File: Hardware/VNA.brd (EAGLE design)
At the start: 122 x 96 mm, 513 parts, among them IC1 ADL5801, IC10 LT5560, IC11 THS4521IDGKR, IC12 MCP33131D-10-E/MS, IC13 SI5351C, IC14 MAX2871, IC15 NCP702-3.3, IC16 RFSW6042, IC17 AP2114H, IC18 RFSW6042, IC19 MAX2871, IC2 LT5560, IC20 NCP702-3.3, IC21 AP2114H, IC22 QPC6324, IC23 RFSA3714, IC24 TRF37A73, IC25 QPC6324, IC26 QPC6324, IC27 QPC6324, IC28 LDL212PU50R, IC29 LDL212PU50R, IC3 THS4521IDGKR, IC30 LDL212PU50R, IC31 LDL212PU50R, IC32 TPS65265, IC34 NCP702-1.8, IC35 NCP702-1.8, IC36 NCP702-1.8, IC37 ADL5801, IC4 MCP33131D-10-E/MS, IC5 ADL5801, IC6 LT5560, IC7 THS4521IDGKR, IC8 MCP33131D-10-E/MS, IC9 STM32G431CB, J1 AMPHENOL_132289, J2 AMPHENOL_132289, J3 DCJ0202, J4 TYPE-C16P(073), Q1 FA-128 26MHz, T1 B012-617DB-1-63-B331, T2 B012-617DB-1-63-B331, T3 B012-617DB-1-63-B331, U2 6SLX9TQG144, U4 W25Q16BVSN, X4 DNP

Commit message: library update
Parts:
- C1, C10, C100, C101, C102, C103, C104, C105, C107, C108, C109, C11, C110, C111, C112, C114, C115, C116, C117, C118, C119, C12, C120, C121, C122, C127, C128, C129, C13, C130, C131, C132, C133, C134, C135, C136, C137, C138, C14, C143, C144, C145, C146, C147, C148, C149, C15, C150, C151, C152, C153, C154, C155, C156, C157, C16, C167, C17, C175, C176, C178, C179, C18, C182, C183, C186, C187, C188, C19, C191, C192, C193, C194, C195, C196, C197, C198, C199, C2, C20, C200, C201, C202, C203, C204, C205, C206, C207, C208, C209, C21, C210, C211, C212, C213, C214, C215, C216, C217, C218, C219, C22, C220, C221, C222, C223, C224, C225, C226, C227, C228, C23, C24, C25, C26, C27, C28, C29, C3, C30, C31, C32, C33, C34, C35, C36, C37, C38, C39, C4, C40, C41, C42, C43, C44, C45, C46, C47, C48, C49, C5, C50, C51, C52, C53, C54, C55, C56, C57, C58, C59, C6, C60, C61, C62, C63, C64, C65, C66, C67, C68, C69, C7, C70, C71, C72, C73, C74, C75, C76, C77, C78, C79, C8, C80, C81, C82, C83, C84, C85, C86, C87, C88, C89, C9, C90, C91, C92, C93, C94, C95, C96, C97, C98, C99: device rcl:C0402 -> VNA:C0402
- D1, D2: device diodes:SMB -> VNA:SMB
- IC1, IC37, IC5: device rf:QFN50P400X400X100-25T250N -> VNA:QFN50P400X400X100-25T250N
- IC11, IC3, IC7: device rf:MSOP8 -> VNA:MSOP8
- IC22, IC25, IC26, IC27: device rf:QFN50P400X400X75-21T206 -> VNA:QFN50P400X400X75-21T206
- IC23: device rf:QFN50P400X400X75-25T270 -> VNA:QFN50P400X400X75-25T270
- IC9: device custom-ic:QFN50P700X700X60-49T560N -> VNA:QFN50P700X700X60-49T560N
- J1, J2: device custom-connectors:AMPHENOL_132289 -> VNA:AMPHENOL_132289
- J4: device custom-connectors:TYPE-C16P -> VNA:TYPE-C16P
- JP1: device pinhead:2X10 -> VNA:2X10
- JP2: device pinhead:1X10/90 -> VNA:1X10/90
- L1, L10, L11, L12, L13, L14, L15, L16, L17, L18, L19, L2, L20, L21, L22, L23, L24, L25, L26, L27, L28, L3, L31, L32, L33, L34, L35, L36, L37, L38, L39, L4, L40, L41, L42, L43, L44, L45, L46, L47, L48, L49, L5, L50, L6, L7, L8, L9: device rf:R0402 -> VNA:R0402:1
- LED1, LED10, LED2, LED3, LED4, LED5, LED6, LED7, LED8, LED9: device led:CHIPLED_0603 -> VNA:CHIPLED_0603
- R1, R10, R100, R101, R102, R103, R104, R105, R106, R107, R108, R109, R11, R110, R111, R112, R113, R114, R115, R116, R117, R118, R119, R12, R120, R121, R122, R123, R124, R125, R126, R127, R128, R129, R13, R130, R131, R132, R133, R134, R135, R136, R137, R138, R139, R14, R140, R141, R142, R143, R144, R145, R146, R147, R148, R15, R16, R17, R18, R19, R2, R20, R21, R22, R23, R24, R25, R26, R27, R28, R29, R3, R30, R31, R32, R33, R34, R35, R36, R37, R38, R39, R4, R40, R41, R42, R43, R44, R45, R46, R47, R48, R49, R5, R50, R51, R52, R53, R54, R55, R56, R57, R58, R59, R6, R60, R61, R62, R63, R64, R65, R66, R67, R69, R7, R70, R71, R72, R73, R74, R75, R76, R77, R78, R79, R8, R80, R81, R82, R83, R84, R85, R86, R87, R88, R89, R9, R90, R91, R92, R93, R94, R95, R96, R97, R98, R99: device rcl:R0402 -> VNA:R0402
- T1, T2, T3: device rf:EASTEVER_BALUN -> VNA:EASTEVER_BALUN
- TP1, TP10, TP11, TP12, TP13, TP14, TP15, TP16, TP17, TP18, TP19, TP2, TP3, TP4, TP5, TP6, TP7, TP8, TP9: device testpad:B1,27 -> VNA:B1,27
- X5, X6: value (none) -> SMA_CONNECTOR

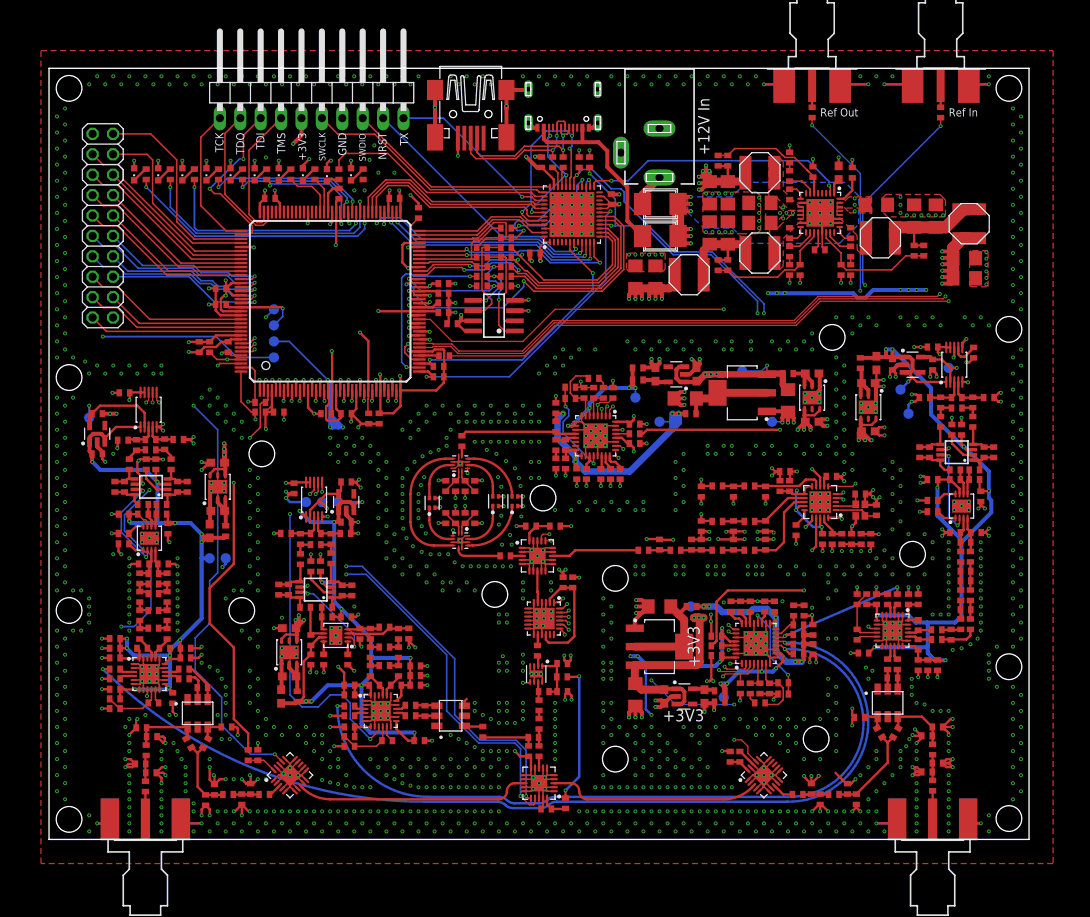
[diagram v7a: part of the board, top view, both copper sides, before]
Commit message: reworked power supply section
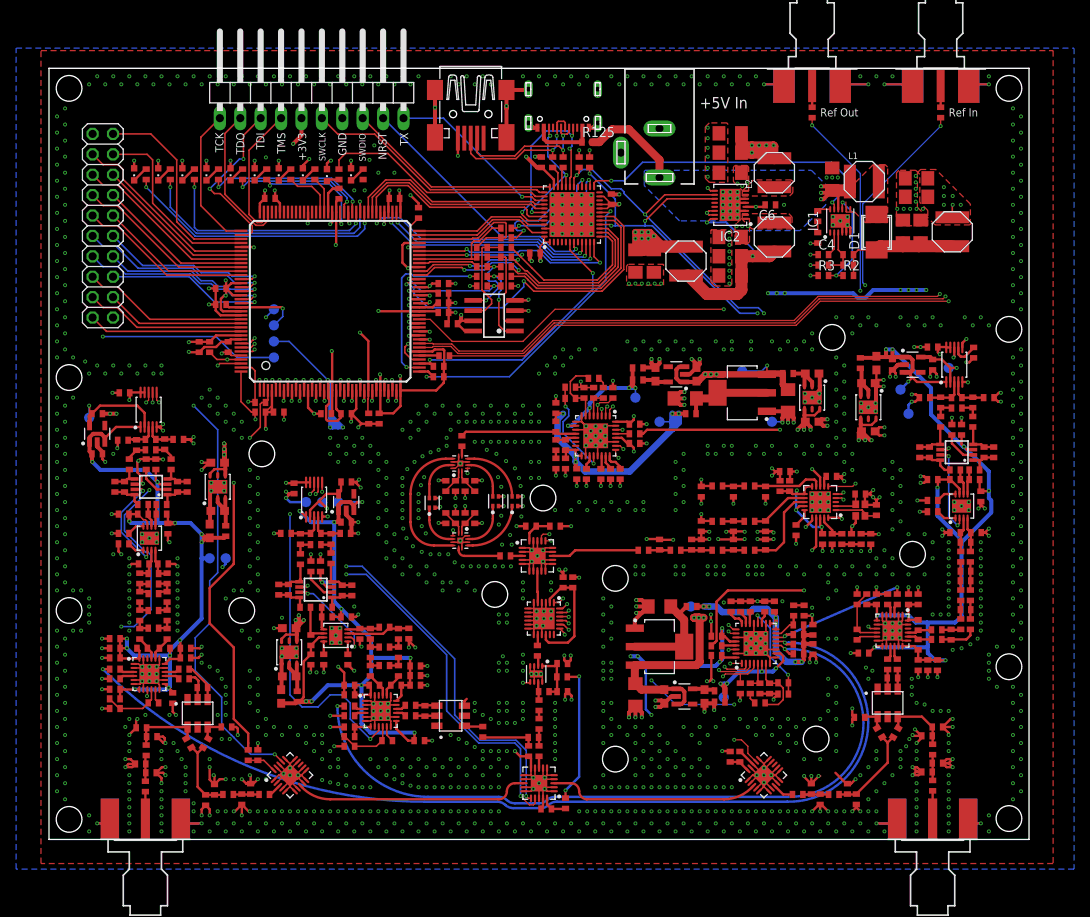
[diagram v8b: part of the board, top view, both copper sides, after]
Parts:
- removed C223: 56p, VNA:C0402
- removed C224, C225, C226, C227, C228: 100n, VNA:C0402
- removed D2: MBRS2040LT3G, VNA:SMB
- removed L54: 6u8, VNA:SRN5040
- removed L55: 10u, VNA:SRN5040
- removed R143, R144, R145, R146, R147: 0, VNA:R0402
- removed R148: 330, VNA:R0402
- added IC33: ADL5801, VNA:QFN50P400X400X100-25T250N
- added L29: Ferrite, VNA:R0402:1
- added L30: 330n, VNA:R0402:1
- added R68: 620, VNA:R0402
- C1, C2, C3: value 100n/RF -> 10u; device VNA:C0402 -> VNA:C1206
- C10, C11, C8: value 10n -> 10u; device VNA:C0402 -> VNA:C1206
- C100: value 18p -> 1u
- C101: value 56p -> 1u
- C102, C103, C118, C97: value 18p -> 100n
- C104, C105, C120, C143, C148, C157, C191, C192, C30, C39, C80: value 100n -> 10n
- C106, C123, C160: value 1u -> 10n; device VNA:C0603 -> VNA:C0402
- C107: value 10n -> DNP
- C108: value 4p -> 1u
- C109: value 4p -> 100n/RF
- C110, C71, C96: value 100n -> 100n/RF
- C111: value 56p -> 10n
- C112: value 18p -> DNP
- C113: value 4u7 -> DNP; device VNA:C0603 -> VNA:C0402
- C114, C115, C116, C122, C134, C193, C73: value 1u -> 100n
- C117, C135, C222: value 180p -> 100n
- C119: value 3n3 -> 100n
- C12, C13, C15, C49, C7: value 100n -> 10u; device VNA:C0402 -> VNA:C1206
- C121: value 100n/RF -> 330p
- C124: value 1u -> 120p; device VNA:C0603 -> VNA:C0402
- C125, C126: value 10u -> 330p; device VNA:C1206 -> VNA:C0402
- C127: value 100n -> 330p
- C128, C196: value 100n -> 150p
- C129, C131, C138, C145, C198, C203, C59: value 100n -> 1u
- C130: value 10n -> 33p
- C132, C153, C33, C4: value 100n/RF -> 100n
- C133: value 1u -> 100n/RF
- C136, C99: value 18p -> 100n/RF
- C137: value 3n3 -> 1u
- C139, C140: value 1u -> 100n; device VNA:C0603 -> VNA:C0402
- C14: value 120p -> 10u; device VNA:C0402 -> VNA:C1206
- C141, C142: value 10u -> 10n; device VNA:C1206 -> VNA:C0402
- C144, C149: value 100n -> DNP
- C146, C147, C65, C74: value 10n -> 100n/RF
- C150: value 100n/RF -> DNP
- C158, C162, C164: value 1u -> 330p; device VNA:C0603 -> VNA:C0402
- C159: value 4u7 -> 100n; device VNA:C0603 -> VNA:C0402
- C16, C17, C53: value 330p -> 10u; device VNA:C0402 -> VNA:C1206
- C161: value 4u7 -> 120p; device VNA:C0603 -> VNA:C0402
- C163: value 4u7 -> 330p; device VNA:C0603 -> VNA:C0402
- C165: value 1u -> 150p; device VNA:C0603 -> VNA:C0402
- C166, C168: device VNA:C0603 -> VNA:C0402
- C167, C197: value 100n -> 33p
- C169, C181, C190: value 22u -> 100n; device VNA:C1206 -> VNA:C0402
- C170: value 22u -> 100n/RF; device VNA:C1206 -> VNA:C0402
- C171, C172, C180: value 22u -> 10n; device VNA:C1206 -> VNA:C0402
- C173: value 10u/25V -> DNP; device VNA:C1206 -> VNA:C0402
- C174: value 22u -> DNP; device VNA:C1206 -> VNA:C0402
- C175: value 47n -> 10n
- C176: value 1n -> DNP
- C177: value 10u/25V -> 1u; device VNA:C1206 -> VNA:C0402
- C178: value 47n -> 100n/RF
- C179: value 8p2 -> 100n/RF
- C18, C26, C52, C81: value 100n -> 1u; device VNA:C0402 -> VNA:C0603
- C182, C56: value 120p -> 100n
- C183, C69, C83: value DNP -> 100n
- C184, C189: value 22u -> 330p; device VNA:C1206 -> VNA:C0402
- C185: value 10u/25V -> 100n; device VNA:C1206 -> VNA:C0402
- C186: value 47n -> 100n
- C187: value 510p -> 330p
- C188: value DNP -> 330p
- C19, C27: value 330p -> 1u; device VNA:C0402 -> VNA:C0603
- C194: value 1u -> 120p
- C20, C21, C28, C79: device VNA:C0402 -> VNA:C0603
- C200, C201, C213, C214, C215, C217, C218, C219, C55, C72: value 10n -> 100n
- C202, C87: value 10n -> 1u
- C22, C23: value 100n -> 4u7; device VNA:C0402 -> VNA:C0603
- C221, C98: value 56p -> 100n
- C24, C25: value DNP -> 4u7; device VNA:C0402 -> VNA:C0603
- C31: value 150p -> 4p
- C32: value 33p -> 100n
- C34: value 100n/RF -> 4p
- C35, C36, C67: value 100n/RF -> 18p
- C37: value DNP -> 18p
- C38: value 100n -> 56p
- C40, C42: value 10n -> 56p
- C41, C47: value 1u -> 56p
- C43: value 100n -> 180p
- C44, C45: value 100n -> 18p
- C46, C95: value 1u -> 18p
- C5, C51: value DNP -> 10n
- C50: value DNP -> 1u; device VNA:C0402 -> VNA:C0603
- C57: value 150p -> 100n
- C58: value 33p -> 1u
- C60: value 330p -> 1u
- C61, C62, C85, C94: value 330p -> 100n
- C63: value 1u -> 180p
- C66: value 100n/RF -> 3n3
- C78: value 1u -> 10u; device VNA:C0402 -> VNA:C1206
- C82: value DNP -> 10u; device VNA:C0402 -> VNA:C1206
- C88: value 120p -> 1u
- C89: value 150p -> 1u
- C9: value 1u -> 100p
- C90: value 33p -> 180p
- C92: value 330p -> 3n3
- C93: value 330p -> 10n
- IC1: value ADL5801 -> MIC2253; device VNA:QFN50P400X400X100-25T250N -> VNA:SON50P300X300X90-13T170X240N
- IC10: value LT5560 -> MAX2871; device VNA:SON50P300X300X80-9T165X238 -> VNA:QFN50P500X500X80-33T310
- IC11: value THS4521IDGKR -> RFSW6042; device VNA:MSOP8 -> VNA:QFN40P180X180X55-13T76N
- IC12: value MCP33131D-10-E/MS -> RFSW6042; device VNA:SOP50P490X110-10N -> VNA:QFN40P180X180X55-13T76N
- IC13: value SI5351C -> QPC6324; device VNA:QFN50P400X400X90-21T270N -> VNA:QFN50P400X400X75-21T206
- IC14: value MAX2871 -> RFSA3714; device VNA:QFN50P500X500X80-33T310 -> VNA:QFN50P400X400X75-25T270
- IC15: value NCP702-3.3 -> TRF37A73; device VNA:SOT95P240X110-5 -> VNA:SON50P200X200X80-9T90X160N
- IC16, IC18: value RFSW6042 -> QPC6324; device VNA:QFN40P180X180X55-13T76N -> VNA:QFN50P400X400X75-21T206
- IC17: value AP2114H -> QPC6324; device VNA:SOT230P700X180-4 -> VNA:QFN50P400X400X75-21T206
- IC19: value MAX2871 -> AP2114H; device VNA:QFN50P500X500X80-33T310 -> VNA:SOT230P700X180-4
- IC2: value LT5560 -> LM3370SD-4221; device VNA:SON50P300X300X80-9T165X238 -> VNA:SON50P400X500X80-17T260X400N
- IC21: value AP2114H -> MAX2871; device VNA:SOT230P700X180-4 -> VNA:QFN50P500X500X80-33T310
- IC22, IC27: value QPC6324 -> LT5560; device VNA:QFN50P400X400X75-21T206 -> VNA:SON50P300X300X80-9T165X238
- IC23: value RFSA3714 -> THS4521IDGKR; device VNA:QFN50P400X400X75-25T270 -> VNA:MSOP8
- IC24: value TRF37A73 -> ADL5801; device VNA:SON50P200X200X80-9T90X160N -> VNA:QFN50P400X400X100-25T250N
- IC25: value QPC6324 -> NCP702-1.8; device VNA:QFN50P400X400X75-21T206 -> VNA:SOT95P240X110-5
- IC26: value QPC6324 -> MCP33131D-10-E/MS; device VNA:QFN50P400X400X75-21T206 -> VNA:SOP50P490X110-10N
- IC28: value LDL212PU50R -> THS4521IDGKR; device VNA:SON95P300X300X100-7T170X240N -> VNA:MSOP8
- IC29: value LDL212PU50R -> ADL5801; device VNA:SON95P300X300X100-7T170X240N -> VNA:QFN50P400X400X100-25T250N
- IC3: value THS4521IDGKR -> LDL212PU50R; device VNA:MSOP8 -> VNA:SON95P300X300X100-7T170X240N
- IC30: value LDL212PU50R -> NCP702-1.8; device VNA:SON95P300X300X100-7T170X240N -> VNA:SOT95P240X110-5
- IC31: value LDL212PU50R -> MCP33131D-10-E/MS; device VNA:SON95P300X300X100-7T170X240N -> VNA:SOP50P490X110-10N
- IC32: value TPS65265 -> THS4521IDGKR; device VNA:QFN50P500X500X100-33T345N -> VNA:MSOP8
- IC35: value NCP702-1.8 -> MCP33131D-10-E/MS; device VNA:SOT95P240X110-5 -> VNA:SOP50P490X110-10N
- IC36: value NCP702-1.8 -> LT5560; device VNA:SOT95P240X110-5 -> VNA:SON50P300X300X80-9T165X238
- IC37: value ADL5801 -> STM32G431CB; device VNA:QFN50P400X400X100-25T250N -> VNA:QFN50P700X700X60-49T560N
- IC4: value MCP33131D-10-E/MS -> LDL212PU50R; device VNA:SOP50P490X110-10N -> VNA:SON95P300X300X100-7T170X240N
- IC5: value ADL5801 -> LDL212PU50R; device VNA:QFN50P400X400X100-25T250N -> VNA:SON95P300X300X100-7T170X240N
- IC6: value LT5560 -> LDL212PU50R; device VNA:SON50P300X300X80-9T165X238 -> VNA:SON95P300X300X100-7T170X240N
- IC7: value THS4521IDGKR -> SI5351C; device VNA:MSOP8 -> VNA:QFN50P400X400X90-21T270N
- IC8: value MCP33131D-10-E/MS -> AP2114H; device VNA:SOP50P490X110-10N -> VNA:SOT230P700X180-4
- IC9: value STM32G431CB -> NCP702-3.3; device VNA:QFN50P700X700X60-49T560N -> VNA:SOT95P240X110-5
- J1: value AMPHENOL_132289 -> DNP; device VNA:AMPHENOL_132289 -> VNA:DCJ0202
- J3: value DCJ0202 -> AMPHENOL_132289; device VNA:DCJ0202 -> VNA:AMPHENOL_132289
- JP1: device VNA:2X10 -> VNA:1X10/90
- JP2: device VNA:1X10/90 -> VNA:2X10
- L1, L2, L3: value 330n -> 2u2; device VNA:R0402:1 -> VNA:SRN5040
- L10, L25, L26, L9: value 33n -> Ferrite
- L11, L12, L17: value 330n -> 120n
- L13: value 68n -> 120n
- L14, L24: value 68n -> 330n
- L15, L16: value 33n -> 120n
- L19, L20, L21, L22, L27, L28, L6: value 330n -> Ferrite
- L23, L7, L8: value 68n -> Ferrite
- L31, L38, L39, L40, L41, L46, L47: value Ferrite -> 330n
- L32, L33: value 120n -> 330n
- L34, L35: value 120n -> 68n
- L36, L37: value 120n -> 33n
- L4, L5: value Ferrite -> 2u2; device VNA:R0402:1 -> VNA:SRN5040
- L42, L43, L48, L49: value Ferrite -> 68n
- L44: value 330n -> 33n
- L45, L50: value Ferrite -> 33n
- L51: value 10u -> 33n; device VNA:SRN5040 -> VNA:R0402:1
- L52, L53: value 6u8 -> 330n; device VNA:SRN5040 -> VNA:R0402:1
- LED1, LED5: value Green -> Red
- LED10, LED2: value Red -> Green
- LP2: value LP0603A1880ANTR -> LP0603N3500ANTR
- LP3: value LP0603N3500ANTR -> LP0603A1880ANTR
- R10: value 620 -> 5k1
- R100, R111, R112, R113: value 10k -> DNP
- R101: value 10k -> 1k
- R102, R103, R80, R86, R97, R98, R99: value 10k -> 220
- R104, R49: value 10k -> 0
- R105, R106, R107, R108, R109, R110: value 330 -> 0
- R11, R25: value 1k -> 10k
- R116, R127, R128, R130, R131: value DNP -> 10k
- R117, R121, R122, R19, R20, R31: value 220 -> 10k
- R118, R119: value 220 -> 20
- R12: value 18 -> 49R9
- R120: value 220 -> 330
- R123, R126, R91: value DNP -> 20
- R124: value 0 -> 20
- R125, R77: value DNP -> 0
- R129: value 0 -> 10k
- R13: value 620 -> 49R9
- R134: value 10k -> 330
- R135, R136, R39: value 20 -> 330
- R137, R138, R139, R140: value DNP -> 330
- R14: value 330 -> 49R9
- R141, R142: value 0 -> 330
- R15: value 200 -> 1k8
- R16: value 200 -> 82
- R17: value 6k8 -> 330
- R18: value 6k8 -> 10k
- R2: value 620 -> 4k7
- R21, R5: value 620 -> 10k
- R22, R23, R24, R6: value 49R9 -> 10k
- R26: value 330 -> 2R7
- R27: value 200 -> 406
- R28: value 200 -> 56
- R29: value 6k8 -> 2R7
- R3: value 18 -> 10k
- R30: value 6k8 -> 5k1
- R32: value 220 -> 49R9
- R33, R72: value 56 -> 49R9
- R34, R35, R38, R76: value 20 -> 49R9
- R36: value 56 -> 1k8
- R37: value 56 -> 82
- R4: value 620 -> 38k3
- R40: value 56 -> 620
- R41: value 1k -> 620
- R42: value 330 -> 18
- R43, R44: value 200 -> 620
- R45, R46: value 4k7 -> 49R9
- R47, R48: value 220 -> DNP
- R50: value 1k8 -> 49R9
- R51: value 82 -> DNP
- R52: value 330 -> DNP
- R53, R61: value 5k1 -> 220
- R54, R62: value 49R9 -> 220
- R55: value 49R9 -> 6k8
- R56, R83: value 10k -> 6k8
- R57: value 49R9 -> DNP
- R58: value 1k8 -> 220
- R59: value 82 -> 220
- R60: value 330 -> 1k
- R63, R66: value 49R9 -> 56
- R64, R92: value 10k -> 20
- R65: value 49R9 -> 20
- R67: value 49R9 -> 620
- R69: value 2R7 -> 18
- R7: value 49R9 -> 100
- R70: value 2R7 -> 620
- R71: value 406 -> 620
- R73: value 100 -> 49R9
- R74: value 62 -> DNP
- R75: value 100 -> DNP
- R78: value 51k -> DNP
- R79: value 82k -> DNP
- R8: value 49R9 -> 62
- R81: value 91k -> 220
- R82: value 16k -> 6k8
- R84: value 20k -> DNP
- R85: value 30k -> 220
- R87: value 45k3 -> 1k
- R88, R96: value 20 -> 220
- R89: value DNP -> 220
- R9: value 620 -> 100
- R90, R93: value 10k -> 56
- R94, R95: value 10k -> 4k7
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- renumbered U4 to U1, X4 to X3, X5 to X2, X6 to X1
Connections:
- removed net +12V: C173.1, C177.1, C185.1, D1.C, D2.C, IC32.12, IC32.13, IC32.30, IC32.31
- removed net N$167: IC32.32, R77.2
- removed net N$168: C178.2, IC32.25
- removed net N$169: C178.1, IC32.28, IC32.29, L52.P$1
- removed net N$170: C175.2, IC32.9
- removed net N$172: IC32.7, R82.2
- removed net N$174: IC32.23, R79.2
- removed net N$176: C183.2, IC32.22, R80.2, R81.1
- removed net N$178: C179.2, IC32.6, R83.2, R84.1
- removed net N$180: C186.2, IC32.16
- removed net N$182: IC32.18, R85.2
- removed net N$184: C188.2, IC32.19, R86.2, R87.1
- removed net N$226: C187.2, R85.1
- removed net N$227: C176.2, R82.1
- removed net N$232: D1.A, J3.1
- removed net POWER_GOOD: IC32.2, IC9.25
- removed net SWITCHING_SYNC: IC32.20, R78.2
- new net +5V: C1.1, C2.1, C3.1, C6.2, IC1.10, IC2.1, IC2.14, IC2.15, IC2.4, IC2.8, J1.1, L1.P$1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
- new net EN_6V: IC1.11, IC37.25
- new net N$158: C9.2, IC1.3, R4.1, R5.2
- new net N$165: C4.2, IC1.2
- new net N$34: D1.A, IC1.7, IC1.8, L1.P$2
- new net N$65: IC1.12, R1.2
- net +3V3: now also C132.2, C14.1, C15.1, C169.2, C201.2, C208.1, C209.1, C210.1, C212.1, C214.1, C216.1, C218.1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; no longer C110.2, C120.1, C127.1, C138.1, C143.1, C189.1, C190.1, C191.1, C192.1, C203.1, C204.1, C205.1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
- net +5V/1: now also C102.2, C103.2, C104.1, C105.1, C106.1, C108.1, C111.1, C115.2, C119.1, C122.1, C129.1, C26.2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; no longer C12.1, C13.1, C164.2, C193.1, C200.1, C201.1, C202.1, C22.2, C23.2, C30.2, C8.1, C9.1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
- net +5V/2: now also C139.2, C140.2, C141.1, C142.1, C143.1, C145.1, C148.1, C152.2, C156.1, C159.1, C166.1, C27.2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; no longer C165.2, C213.1, C214.1, C215.1, C28.1, C40.1, C41.1, C43.1, C44.1, C48.2, C49.2, C54.2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
- net +5V/3: now also C171.1, C172.1, C175.1, C177.1, C180.1, C181.2, C190.1, C193.1, C195.1, C204.2, C205.2, C28.2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; no longer C166.2, C217.1, C218.1, C219.1, C72.1, C73.1, C75.1, C76.1, C80.2, C81.2, C86.2, C95.1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
- net +5V/4: now also C49.1, C50.1, C78.1, C79.1, IC19.3, IC8.3, IC9.1, IC9.3, L9.2, TP11.TP; no longer C123.1, C125.1, C139.1, C141.1, IC15.1, IC15.3, IC17.3, IC21.3, L50.2, TP13.TP
- net AMP_PWDN: now also IC15.5; no longer IC24.5
- net ATT_D0: now also IC14.1; no longer IC23.1
- net ATT_D1: now also IC14.24; no longer IC23.24
- net ATT_D2: now also IC14.23; no longer IC23.23
- net ATT_D3: now also IC14.22; no longer IC23.22
- net ATT_D4: now also IC14.21; no longer IC23.21
- net ATT_D5: now also IC14.20; no longer IC23.20
- net ATT_D6: now also IC14.19; no longer IC23.19
- net FILT_IN_C1: now also R21.2; no longer R99.2
- net FILT_IN_C2: now also R20.2; no longer R100.2
- net FILT_OUT_C1: now also R24.2; no longer R104.2
- net FILT_OUT_C2: now also R22.2; no longer R103.2
- net FPGA_CCLK: now also R109.2, R111.2; no longer R146.2, R91.2
- net FPGA_CLK: now also IC7.15, R126.1; no longer IC13.15, R96.1
- net FPGA_CSO_B: now also R114.2; no longer R139.2
- net FPGA_DIN: now also R110.2, R113.2; no longer R138.2, R147.2
- net FPGA_DONE: now also IC37.47, R129.1; no longer IC9.47, R92.1
- net FPGA_INIT_B: now also IC37.6, R128.1; no longer IC9.6, R93.1
- net FPGA_M1: now also R108.2, R115.1; no longer R140.1, R141.2
- net FPGA_MOSI: now also R112.2; no longer R137.2
- net FPGA_PROGRAM_B: now also IC37.19, R127.1; no longer IC9.19, R94.1
- net FPGA_RESET: now also IC37.45; no longer IC9.45
- net GND: now also C1.2, C10.2, C102.1, C103.1, C104.2, C105.2, C106.2, C108.2, C11.2, C115.1, C119.2, C125.1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; no longer C100.2, C101.2, C102.2, C103.2, C104.1, C105.1, C106.1, C108.1, C109.1, C110.1, C112.2, C113.1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
- net HIGHBAND_SELECT: now also IC13.17; no longer IC22.17
- net LO1_CE: now also IC21.4, R31.2; no longer IC19.4, R64.2
- net LO1_CLK: now also IC21.1; no longer IC19.1
- net LO1_LD: now also IC21.25; no longer IC19.25
- net LO1_LE: now also IC21.3; no longer IC19.3
- net LO1_MOSI: now also IC21.2; no longer IC19.2
- net LO1_MUX: now also IC21.30; no longer IC19.30
- net LO1_REF: now also C80.1, IC7.17; no longer C146.1, IC13.17
- net LO1_RF_EN: now also IC21.26; no longer IC19.26
- net LOWBAND_SELECT: now also IC13.16; no longer IC22.16
- net MCU_AUX1: now also IC37.9; no longer IC9.9
- net MCU_AUX2: now also IC37.10; no longer IC9.10
- net MCU_AUX3: now also IC37.11; no longer IC9.11
- net MCU_FLASH_CS: now also IC37.17, R107.1; no longer IC9.17, R142.1
- net MCU_FPGA_CCLK: now also IC37.28, R109.1; no longer IC9.28, R146.1
- net MCU_FPGA_DIN: now also IC37.26, R110.1; no longer IC9.26, R147.1
- net MCU_FPGA_NSS: now also IC37.12; no longer IC9.12
- net MCU_FPGA_UNUSED1: now also IC37.43; no longer IC9.43
- net MCU_FPGA_UNUSED2: now also IC37.41; no longer IC9.41
- net MCU_FPGA_UNUSED3: now also IC37.40; no longer IC9.40
- net MCU_INTR: now also IC37.18; no longer IC9.18
- net MCU_MISO: now also IC37.14, R106.1; no longer IC9.14, R143.1
- net MCU_MOSI: now also IC37.15, R105.1; no longer IC9.15, R144.1
- net MCU_SCK: now also IC37.13, R104.1; no longer IC9.13, R145.1
- net N$1: now also C96.2, R40.1, R41.2, R42.2; no longer C2.2, R1.2, R2.1, R3.2
- net N$10: now also C107.2, C109.1; no longer C3.1, C5.2
- net N$100: now also C22.2, IC3.2, IC3.3, L6.1; no longer C113.2, IC28.2, IC28.3, L47.1
- net N$101: now also C35.1, IC7.19, L11.1; no longer C99.1, IC13.19, L33.1
- net N$102: now also C60.1, IC10.23; no longer C116.1, IC14.23
- net N$103: now also C39.1, IC7.16; no longer C65.1, IC13.16
- net N$104: now also C66.2, R16.1; no longer C119.2, R51.1
- net N$105: now also IC10.5, R16.2, R17.1; no longer IC14.5, R51.2, R52.1
- net N$106: now also IC10.22, R10.2; no longer IC14.22, R53.2
- net N$107: now also C30.1; no longer C107.1
- net N$108: now also C30.2, IC7.6; no longer C107.2, IC13.6
- net N$109: now also C32.2, C33.2, IC7.10, IC7.11, IC7.14, IC7.18, L10.2; no longer C104.2, C105.2, IC13.10, IC13.11, IC13.14, IC13.18, L31.2
- net N$11: now also C117.1, IC24.4; no longer C6.1, IC37.4
- net N$110: now also C56.1, C61.1, C64.1, IC10.16, IC10.17, L19.2, R12.2, R13.2, TP14.TP; no longer C129.1, C196.1, C197.1, IC14.16, IC14.17, L38.2, R54.2, R55.2, TP16.TP
- net N$111: now also C86.1, IC21.10, IC21.6, L29.2, TP15.TP; no longer C144.1, IC19.10, IC19.6, L41.2, TP18.TP
- net N$112: now also IC7.7, R6.2; no longer IC13.7, R49.2
- net N$113: now also C34.2, IC7.1; no longer C109.2, IC13.1
- net N$114: now also C31.2, IC7.2; no longer C108.2, IC13.2
- net N$115: now also C95.2, IC21.20, R36.2; no longer C136.2, IC19.20, R58.2
- net N$116: now also C51.2, IC10.29; no longer C130.2, IC14.29
- net N$117: now also C65.1, IC10.12, R12.1; no longer C132.1, IC14.12, R55.1
- net N$118: now also C62.2, IC10.13, R13.1; no longer C131.2, IC14.13, R54.1
- net N$119: now also C62.1, R14.2; no longer C131.1, R57.2
- net N$12: now also C114.2, IC24.3; no longer C7.2, IC37.3
- net N$120: now also C65.2, IC11.7; no longer C132.2, IC16.7
- net N$121: now also IC11.9, IC12.6; no longer IC16.9, IC18.6
- net N$122: now also IC11.11; no longer IC16.11
- net N$123: now also IC12.4; no longer IC18.4
- net N$124: now also IC12.11, LP2.1; no longer IC18.11, LP3.1
- net N$125: now also IC12.9, LP3.1; no longer IC18.9, LP2.1
- net N$126: now also IC11.6, LP3.4; no longer IC16.6, LP2.4
- net N$127: now also IC11.4, LP2.4; no longer IC16.4, LP3.4
- net N$128: now also C53.1, IC8.2, IC8.4, L19.1; no longer C126.1, IC17.2, IC17.4, L38.1
- net N$129: now also C52.1, IC9.5, L20.1; no longer C124.1, IC15.5, L39.1
- net N$13: now also C125.2, C126.1, IC26.3, R61.1; no longer C16.1, C17.2, IC4.3, R117.1
- net N$130: now also C68.1, IC12.7; no longer C121.1, IC18.7
- net N$131: now also C90.1, C92.1, IC21.7, R36.1; no longer C135.1, C137.1, IC19.7, R58.1
- net N$132: now also C87.1, IC21.24; no longer C122.1, IC19.24
- net N$133: now also C88.1, IC21.19; no longer C133.1, IC19.19
- net N$134: now also C89.1, IC21.23; no longer C134.1, IC19.23
- net N$135: now also C92.2, R37.1; no longer C137.2, R59.1
- net N$136: now also IC21.5, R37.2, R39.1; no longer IC19.5, R59.2, R60.1
- net N$137: now also IC21.22, R30.2; no longer IC19.22, R61.2
- net N$138: now also C85.1, C91.1, C94.1, IC21.16, IC21.17, L28.2, R32.2, R33.2, R34.2, R35.2, TP16.TP; no longer C145.1, C198.1, C199.1, IC19.16, IC19.17, L40.2, R62.2, R63.2, R65.2, R66.2, TP19.TP
- net N$139: now also C80.2, IC21.29; no longer C146.2, IC19.29
- net N$14: now also C120.1, IC24.20, L32.2; no longer C11.1, IC37.20, L1.2
- net N$140: now also C69.1, IC13.20, L21.2; no longer C149.1, IC22.20, L42.2
- net N$141: now also C93.1, R38.2; no longer C147.1, R67.2
- net N$142: now also C82.1, IC19.2, IC19.4, L28.1; no longer C142.1, IC21.2, IC21.4, L40.1
- net N$143: now also C81.1, L29.1; no longer C140.1, L41.1
- net N$144: now also IC13.8, IC14.5; no longer IC22.8, IC23.5
- net N$145: now also C70.1, IC14.16, IC14.2, L22.2; no longer C148.1, IC23.16, IC23.2, L43.2
- net N$146: now also C71.1, IC14.14; no longer C150.1, IC23.14
- net N$147: now also C93.2, IC21.15, R35.1; no longer C147.2, IC19.15, R66.1
- net N$148: now also C71.2, IC15.2; no longer C150.2, IC24.2
- net N$149: now also C74.1, IC15.7, L24.2; no longer C153.1, IC24.7, L44.2
- net N$15: now also C123.1, IC24.21, L33.2; no longer C10.1, IC37.21, L2.2
- net N$150: now also C74.2, R26.1; no longer C153.2, R69.1
- net N$151: now also IC16.8, R29.2; no longer IC25.8, R70.2
- net N$152: now also C72.1, C73.1, IC15.1, L23.2, L24.1; no longer C151.1, C152.1, IC24.1, L44.1, L45.2
- net N$153: now also R26.2, R27.2, R29.1; no longer R69.2, R70.1, R71.2
- net N$154: now also IC16.13, IC18.8; no longer IC25.13, IC26.8
- net N$155: now also IC16.3, IC17.3; no longer IC25.3, IC27.3
- net N$156: now also C76.1, IC18.20, L27.2; no longer C156.1, IC26.20, L46.2
- net N$157: now also C38.1, IC7.13, L14.1; no longer C223.1, IC13.13, L20.1
- net N$159: now also C48.2, R8.2, R9.2; no longer C157.2, R74.2, R75.2
- net N$16: now also C123.2, C124.2, L35.1; no longer C10.2, C14.2, L8.1
- net N$160: now also C37.1, IC7.9, L13.1; no longer C112.1, IC13.9, L37.1
- net N$161: now also C23.2, IC4.2, IC4.3, L7.1; no longer C159.2, IC29.2, IC29.3, L48.1
- net N$162: now also IC1.9, R2.1, R3.2; no longer C168.2, IC32.1
- net N$163: now also C16.1, C17.1, C18.2, C19.2, C20.2, C21.2, IC3.4, IC3.6, IC4.4, IC4.6, IC5.4, IC5.6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; no longer C106.2, C158.2, C160.2, C162.2, C174.1, C181.1, IC28.4, IC28.6, IC29.4, IC29.6, IC30.4, IC30.6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
- net N$164: now also C24.2, IC5.2, IC5.3, L8.1; no longer C161.2, IC30.2, IC30.3, L49.1
- net N$166: now also C25.2, IC6.2, IC6.3, L9.1; no longer C163.2, IC31.2, IC31.3, L50.1
- net N$17: now also C128.2, L35.2, L37.1; no longer C31.2, L10.1, L8.2
- net N$171: now also IC2.7, L2.P$1; no longer C175.1, IC32.11, L53.P$1
- net N$175: now also R135.2; no longer R109.2
- net N$177: now also C12.1, C13.1, C9.1, D1.C, L5.P$1, R2.2, R4.2; no longer C170.1, C171.1, C183.1, L51.P$1, L52.P$2, R81.2
- net N$179: now also R136.2; no longer R108.2
- net N$18: now also C98.2, IC22.8; no longer C15.2, IC2.8
- net N$181: now also IC2.2, L3.P$1; no longer C186.1, IC32.14, L54.P$1
- net N$183: now also C11.1, C8.1, IC2.16, L3.P$2, L4.P$1; no longer C180.1, C184.1, C188.1, L54.P$2, L55.P$1, R87.2
- net N$185: now also R125.1; no longer D2.A
- net N$186: now also R119.2; no longer R76.2
- net N$187: now also IC37.33, R118.2; no longer IC9.33, R88.2
- net N$188: now also IC37.34, R119.1; no longer IC9.34, R76.1
- net N$189: now also R118.1; no longer R88.1
- net N$19: now also C118.2, IC24.10, R57.1, R60.2; no longer C212.2, IC37.10, R11.2, R114.1
- net N$190: now also LED1.C, R120.1; no longer LED10.C, R148.1
- net N$191: now also IC37.38, R120.2; no longer IC9.38, R148.2
- net N$194: now also JP2.2; no longer JP1.2
- net N$195: now also JP2.4; no longer JP1.4
- net N$196: now also JP2.3; no longer JP1.3
- net N$197: now also R104.2, R111.1; no longer R145.2, R91.1
- net N$198: now also R126.2; no longer R96.2
- net N$199: now also IC11.2, R18.1, R21.1; no longer IC16.2, R97.1, R99.1
- net N$2: now also R42.1, R43.2, R44.1, R45.2, R46.2; no longer R3.1, R4.2, R5.1, R6.2, R7.2
- net N$20: now also C126.2, C127.1, IC26.4, R62.1; no longer C16.2, C19.1, IC4.4, R118.1
- net N$200: now also IC11.1, R19.1, R20.1; no longer IC16.1, R100.1, R98.1
- net N$201: now also IC12.1, R22.1, R23.1; no longer IC18.1, R101.1, R103.1
- net N$202: now also IC12.2, R24.1, R25.1; no longer IC18.2, R102.1, R104.1
- net N$203: now also C131.1, IC25.5, IC26.2, TP17.TP; no longer C194.1, IC34.5, IC4.2, TP2.TP
- net N$204: now also C168.1, IC30.5, IC31.2, TP18.TP; no longer C63.1, IC35.5, IC8.2, TP4.TP
- net N$205: now also C198.1, IC34.5, IC35.2, TP19.TP; no longer C195.1, IC12.2, IC36.5, TP15.TP
- net N$206: now also LED10.C, R142.1; no longer LED9.C, R14.1
- net N$207: now also LED9.C, R141.1; no longer LED8.C, R26.1
- net N$208: now also LED8.C, R140.1; no longer LED7.C, R42.1
- net N$209: now also LED7.C, R139.1; no longer LED6.C, R105.1
- net N$21: now also C133.2, R67.1, R68.2, R69.2; no longer C34.2, R10.1, R12.2, R9.2
- net N$210: now also LED6.C, R138.1; no longer LED5.C, R106.1
- net N$211: now also LED5.C, R137.1; no longer LED4.C, R107.1
- net N$212: now also LED4.C, R136.1; no longer LED3.C, R108.1
- net N$213: now also LED3.C, R135.1; no longer LED2.C, R109.1
- net N$214: now also LED2.C, R134.1; no longer LED1.C, R110.1
- net N$215: now also R142.2; no longer R14.2
- net N$216: now also R141.2; no longer R26.2
- net N$217: now also IC22.4, L31.1, R64.1, R66.1; no longer IC2.4, L11.1, R34.1, R36.1
- net N$218: now also IC22.3, L30.1, R65.1, R66.2; no longer IC2.3, L3.1, R35.1, R36.2
- net N$219: now also R140.2; no longer R42.2
- net N$22: now also R69.1, R70.2, R71.1, R72.2, R73.2; no longer R12.1, R13.2, R21.1, R22.2, R23.2
- net N$220: now also R139.2; no longer R105.2
- net N$221: now also R138.2; no longer R106.2
- net N$222: now also R137.2; no longer R107.2
- net N$223: now also IC27.4, L39.1, R91.1, R93.1; no longer IC6.4, L18.1, R38.1, R40.1
- net N$224: now also R124.2; no longer R135.2
- net N$225: now also C5.2, R1.1; no longer C182.2, R79.1
- net N$228: now also R123.2; no longer R136.2
- net N$229: now also IC24.11, R57.2; no longer IC37.11, R114.2
- net N$23: now also IC27.3, L38.1, R92.1, R93.2; no longer IC6.3, L17.1, R39.1, R40.2
- net N$230: now also IC29.11, R84.2; no longer IC1.11, R115.2
- net N$231: now also IC33.11, R100.2; no longer IC5.11, R116.2
- net N$233: now also IC37.31, IC37.44; no longer IC9.31, IC9.44
- net N$234: now also IC37.32, IC37.42; no longer IC9.32, IC9.42
- net N$235: now also C75.1, IC16.20, L25.1; no longer C155.1, IC25.20, L5.1
- net N$236: now also C99.2, R47.2, R49.1, R51.1; no longer C1.2, R124.1, R125.2, R126.1
- net N$237: now also R105.2, R112.1; no longer R137.1, R144.2
- net N$238: now also C136.2, R74.2, R77.1, R78.1; no longer C33.2, R129.1, R130.2, R131.1
- net N$239: now also C136.1, J3.1; no longer C33.1, J2.1
- net N$24: now also C97.2, IC22.1; no longer C18.2, IC2.1
- net N$240: now also R106.2, R113.1; no longer R138.1, R143.2
- net N$241: now also R107.2, R114.1; no longer R139.1, R142.2
- net N$242: now also JP2.6; no longer JP1.6
- net N$243: now also JP2.5; no longer JP1.5
- net N$244: now also JP2.8; no longer JP1.8
- net N$245: now also JP2.7; no longer JP1.7
- net N$246: now also JP2.10; no longer JP1.10
- net N$247: now also JP2.9; no longer JP1.9
- net N$248: now also JP2.12; no longer JP1.12
- net N$249: now also JP2.11; no longer JP1.11
- net N$25: now also R72.1, R75.1, R77.2, R79.2; no longer R127.2, R128.1, R129.2, R22.1
- net N$250: now also JP2.14; no longer JP1.14
- net N$251: now also JP2.13; no longer JP1.13
- net N$252: now also JP2.16; no longer JP1.16
- net N$253: now also JP2.15; no longer JP1.15
- net N$254: now also JP2.18; no longer JP1.18
- net N$255: now also JP2.17; no longer JP1.17
- net N$256: now also JP2.19; no longer JP1.19
- net N$26: now also R73.1, R76.1; no longer R23.1, R24.1
- net N$27: now also C100.1, IC22.6, R53.2; no longer C20.1, IC2.6, R15.2
- net N$28: now also C101.1, IC22.5, R54.2; no longer C21.1, IC2.5, R16.2
- net N$29: now also C146.2, IC29.15; no longer C35.2, IC1.15
- net N$3: now also C120.2, C124.1, L34.1; no longer C11.2, C14.1, L7.1
- net N$30: now also C147.2, IC29.16; no longer C36.2, IC1.16
- net N$31: now also C113.1, IC23.4, R56.1, R59.2; no longer C25.1, IC3.4, R18.1, R19.2
- net N$32: now also C112.2, IC23.5, R55.2, R58.2; no longer C24.2, IC3.5, R17.2, R20.2
- net N$33: now also C128.1, L34.2, L36.1; no longer C31.1, L7.2, L9.1
- net N$35: now also C144.1, C147.1; no longer C36.1, C37.1
- net N$36: now also C144.2, C146.1; no longer C35.1, C37.2
- net N$37: now also C154.1, IC29.4; no longer C38.1, IC1.4
- net N$38: now also C151.2, IC29.3; no longer C39.2, IC1.3
- net N$39: now also C157.1, IC29.20, L40.2; no longer C42.1, IC1.20, L6.2
- net N$4: now also R45.1, R48.1, R49.2, R52.2; no longer R123.1, R124.2, R6.1, R89.2
- net N$40: now also C160.1, IC29.21, L41.2; no longer C55.1, IC1.21, L12.2
- net N$41: now also C155.2, IC29.10, R84.1, R87.2; no longer C216.2, IC1.10, R115.1, R25.2
- net N$42: now also C134.2, IC27.1; no longer C45.2, IC6.1
- net N$43: now also C137.1, IC27.6, R80.2; no longer C46.1, IC6.6, R27.2
- net N$44: now also C138.1, IC27.5, R81.2; no longer C47.1, IC6.5, R28.2
- net N$45: now also C150.1, IC28.4, R83.1, R86.2; no longer C51.1, IC7.4, R30.1, R31.2
- net N$46: now also C149.2, IC28.5, R82.2, R85.2; no longer C50.2, IC7.5, R29.2, R32.2
- net N$47: now also C157.2, C161.1, L42.1; no longer C42.2, C56.1, L13.1
- net N$48: now also C160.2, C161.2, L43.1; no longer C55.2, C56.2, L14.1
- net N$49: now also C165.2, L43.2, L45.1; no longer C57.2, L14.2, L16.1
- net N$5: now also R46.1, R50.1; no longer R7.1, R8.1
- net N$50: now also C165.1, L42.2, L44.1; no longer C57.1, L13.2, L15.1
- net N$51: now also C77.1, IC17.20, L26.2; no longer C154.1, IC27.20, L4.2
- net N$52: now also C135.2, IC27.8; no longer C59.2, IC6.8
- net N$53: now also C162.2, C163.1, IC31.3, R88.1; no longer C60.1, C61.2, IC8.3, R119.1
- net N$54: now also C163.2, C164.1, IC31.4, R89.1; no longer C60.2, C62.1, IC8.4, R120.1
- net N$55: now also C167.1, L44.2, R90.2, R91.2; no longer C58.1, L15.2, R37.2, R38.2
- net N$56: now also C167.2, L45.2, R90.1, R92.2; no longer C58.2, L16.2, R37.1, R39.2
- net N$57: now also C43.1, L14.2, L18.1; no longer C222.1, L19.1, L20.2
- net N$58: now also C138.2, C150.2, IC28.1, R83.2; no longer C47.2, C51.2, IC7.1, R30.2
- net N$59: now also C137.2, C149.1, IC28.8, R82.1; no longer C46.2, C50.1, IC7.8, R29.1
- net N$6: now also C99.1, J2.1; no longer C1.1, J1.1
- net N$60: now also C39.2; no longer C65.2
- net N$61: now also C170.2; no longer C66.2
- net N$62: now also C130.1, L36.2, R63.2, R64.2; no longer C32.1, L9.2, R33.2, R34.2
- net N$63: now also C130.2, L37.2, R63.1, R65.2; no longer C32.2, L10.2, R33.1, R35.2
- net N$64: now also C67.2, IC10.20, R15.2; no longer C118.2, IC14.20, R50.2
- net N$66: now also C178.2, IC33.15; no longer C67.2, IC5.15
- net N$67: now also C179.2, IC33.16; no longer C68.2, IC5.16
- net N$68: now also C176.1, C179.1; no longer C68.1, C69.1
- net N$69: now also C176.2, C178.1; no longer C67.1, C69.2
- net N$7: now also C109.2, IC24.15; no longer C3.2, IC37.15
- net N$70: now also C185.1, IC33.4; no longer C70.1, IC5.4
- net N$71: now also C183.2, IC33.3; no longer C71.2, IC5.3
- net N$72: now also C191.1, IC33.20, L46.2; no longer C74.1, IC5.20, L21.2
- net N$73: now also C192.1, IC33.21, L47.2; no longer C87.1, IC5.21, L22.2
- net N$74: now also C186.2, IC33.10, R100.1, R101.2; no longer C220.2, IC5.10, R116.1, R41.2
- net N$75: now also C199.2, IC36.1; no longer C77.2, IC10.1
- net N$76: now also C202.1, IC36.6, R102.2; no longer C78.1, IC10.6, R43.2
- net N$77: now also C203.1, IC36.5, R103.2; no longer C79.1, IC10.5, R44.2
- net N$78: now also C173.1, C202.2, IC32.8, R94.1; no longer C78.2, C82.1, IC11.8, R45.1
- net N$79: now also C174.2, C203.2, IC32.1, R95.2; no longer C79.2, C83.2, IC11.1, R46.2
- net N$8: now also C110.2, IC24.16; no longer C4.2, IC37.16
- net N$80: now also C174.1, IC32.4, R95.1, R97.2; no longer C83.1, IC11.4, R46.1, R47.2
- net N$81: now also C173.2, IC32.5, R94.2, R96.2; no longer C82.2, IC11.5, R45.2, R48.2
- net N$82: now also C191.2, C194.1, L48.1; no longer C74.2, C88.1, L23.1
- net N$83: now also C192.2, C194.2, L49.1; no longer C87.2, C88.2, L24.1
- net N$84: now also C196.2, L49.2, L51.1; no longer C89.2, L24.2, L26.1
- net N$85: now also C196.1, L48.2, L50.1; no longer C89.1, L23.2, L25.1
- net N$86: now also C197.1, IC36.3, L50.2, L52.1; no longer C90.1, IC10.3, L25.2, L27.1
- net N$87: now also C197.2, IC36.4, L51.2, L53.1; no longer C90.2, IC10.4, L26.2, L28.1
- net N$88: now also C200.2, IC36.8; no longer C91.2, IC10.8
- net N$89: now also C187.2, C188.1, IC35.3, R98.1; no longer C92.1, C93.2, IC12.3, R121.1
- net N$9: now also C107.1, C110.1; no longer C4.1, C5.1
- net N$90: now also C188.2, C189.1, IC35.4, R99.1; no longer C92.2, C94.1, IC12.4, R122.1
- net N$91: now also C40.1, L11.2, L15.1; no longer C98.1, L32.1, L33.2
- net N$92: now also C101.2, C113.2, IC23.1, R56.2; no longer C21.2, C25.2, IC3.1, R18.2
- net N$93: now also C63.1, C66.1, IC10.7, R15.1; no longer C117.1, C119.1, IC14.7, R50.1
- net N$94: now also C58.1, IC10.24; no longer C114.1, IC14.24
- net N$95: now also C100.2, C112.1, IC23.8, R55.1; no longer C20.2, C24.1, IC3.8, R17.1
- net N$96: now also C41.1, L12.2, L16.1; no longer C101.1, L34.1, L35.2
- net N$97: now also C36.1, IC7.12, L12.1; no longer C102.1, IC13.12, L35.1
- net N$98: now also C59.1, IC10.19; no longer C115.1, IC14.19
- net N$99: now also C42.1, L13.2, L17.1; no longer C111.1, L36.1, L37.2
- net NRST: now also IC37.7, JP1.9; no longer IC9.7, JP2.9
- net OUT+: now also C121.1, R58.1, R61.2; no longer C27.1, R117.2, R20.1
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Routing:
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- added copper zone on layer 1, net +5V
- added copper zone on layer 16, net +5V
- added copper zone on layer 16, net GND
- added copper zone on layer 1, net N$163
- added copper zone on layer 1, net N$34
- removed copper zone on layer 1, net +12V
- removed copper zone on layer 16, net +12V
- removed copper zone on layer 1, net N$169
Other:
- board text added: "+5V In"
- board text removed: "+12V In"
